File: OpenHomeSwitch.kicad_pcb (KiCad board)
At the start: 4 copper layers, 82.5 x 65.5 mm, 297 parts, among them J10 USB_C_Receptacle_USB2.0, J11 USB_C_Receptacle_USB2.0, J2 Conn_01x04, J3 Conn_01x04, J4 Micro_SD_Card_Det2, J5 Conn_01x04, J6 Extension I2C, J7 Conn_01x04, J8 Debug, J9 Extension UART, Q1 2N7002, Q10 MMBT3904, Q2 MMBT3904, Q3 MMBT3904, Q4 MMBT5401, Q5 AO3401A, Q6 MMBT5401, Q7 MMBT5401, Q8 AO3401A, Q9 MMBT5401, U1 RTL8367RB, U2 Allwinner_V3S, U3 TMI7003x, U4 TMI7003x, U5 W25Q128JVS, U6 SRV05-4, Y1 25MHz, Y2 24MHz, Y3 32.768kHz

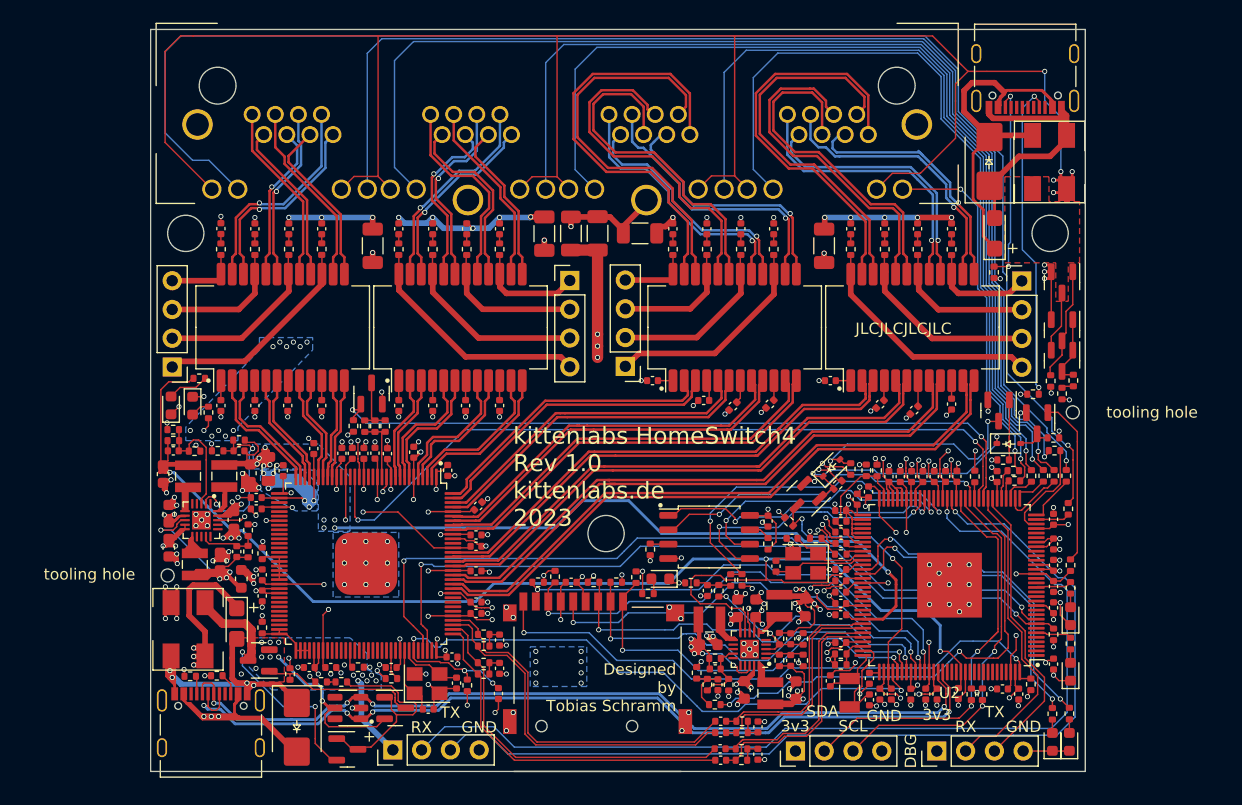
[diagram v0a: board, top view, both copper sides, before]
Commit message: Connect shield net to second USB port
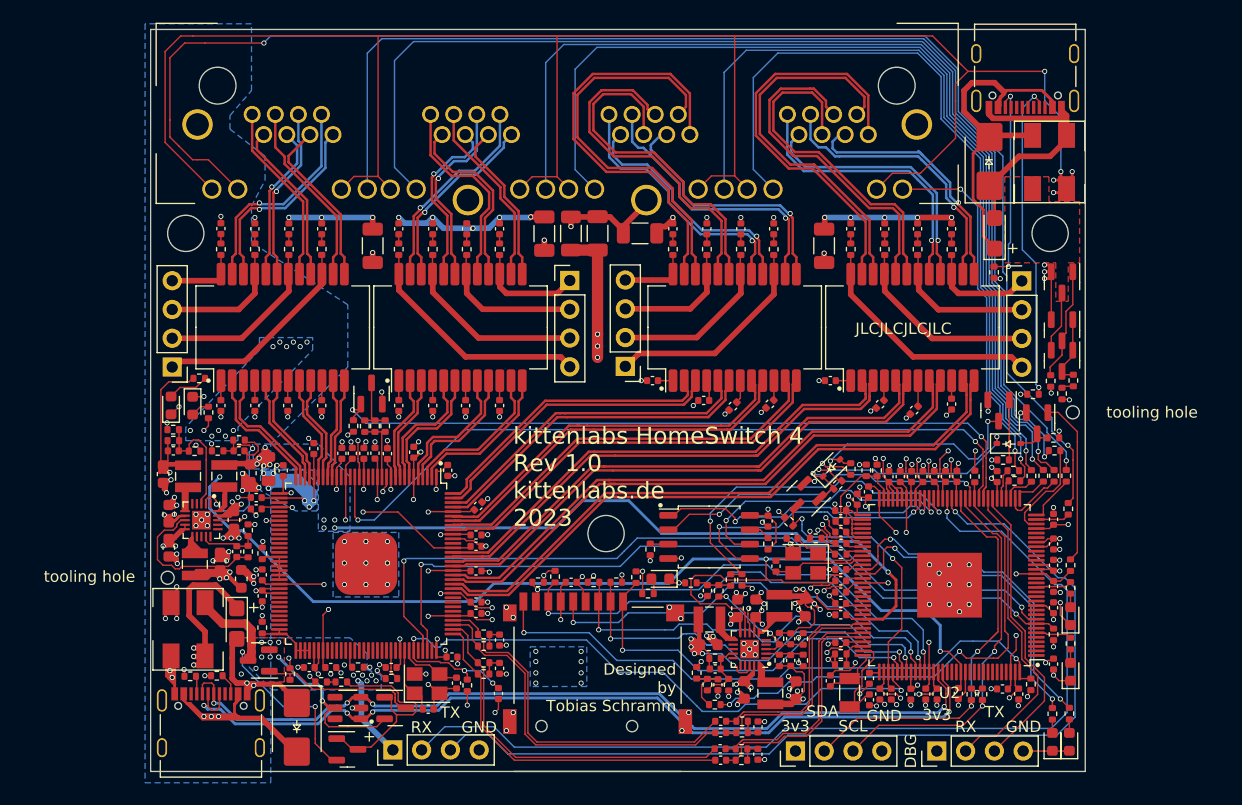
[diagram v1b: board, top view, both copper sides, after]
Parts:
- moved H5 0.20 mm to (145.0, 111.9)
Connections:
- J11 pad A7: /USB2/D- -> /USB2/D2-
- J11 pad B6: /USB2/D+ -> /USB2/D2+
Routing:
- net Net-(D5-A1): track 49.2 -> 39.7 mm
- net +3V0: track 129.7 -> 133.1 mm, vias 3 -> 4
- net GND: track 378.8 -> 375.5 mm, vias 198 -> 197
- net +3V3: track 111.4 -> 112.6 mm, vias 35 -> 34
- net Net-(J1-Pad12): track 130.2 -> 129.3 mm, vias 1 -> 2
- added copper zone on B.Cu, net Earth
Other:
- board text added: "kittenlabs HomeSwitch 4 Rev 1.0 kittenlabs.de 2023"
- board text removed: "kittenlabs HomeSwitch4 Rev 1.0 kittenlabs.de 2023"

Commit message: Fix critical DRC errors
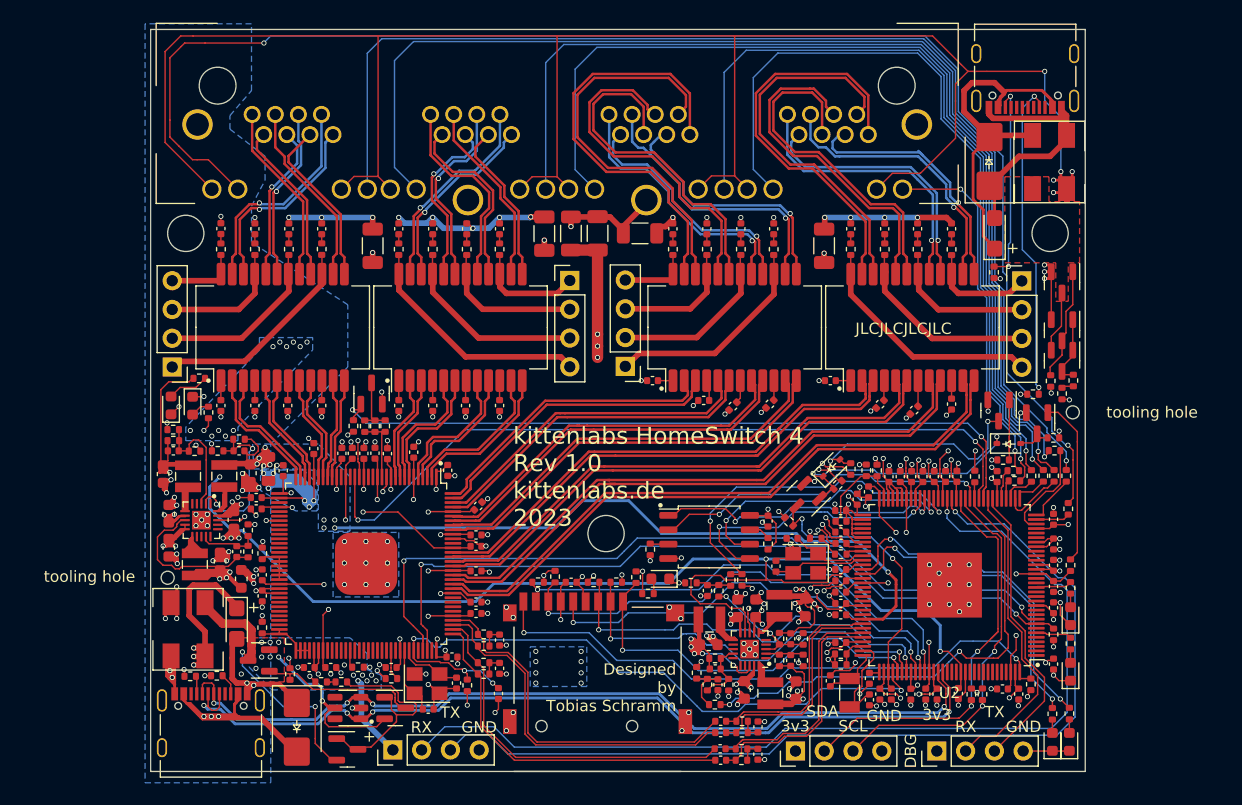
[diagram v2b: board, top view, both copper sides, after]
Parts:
- moved R21 0.08 mm to (151.3, 99.7)
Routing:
- net AVDDL: track 63.6 -> 60.5 mm, vias 14 -> 12
- net AVDDH: track 41.2 -> 39.1 mm, vias 14 -> 13
- net Net-(C32-Pad2): track 14.3 -> 14.0 mm, vias 5 -> 4
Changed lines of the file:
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@@
         (effects (font (size 1 1) (thickness 0.15)))
     )
-    (fp_text user "${REFERENCE}" (at 0 0 90) (layer "F.Fab")
-        (effects (font (size 0.25 0.25) (thickness 0.04)))
-    )
     (fp_line (start -0.107836 -0.36) (end 0.107836 -0.36)
       (stroke (width 0.12) (type solid)) (layer "F.SilkS"))
@@
   )
   (footprint "Resistor_SMD:R_0402_1005Metric" (layer "F.Cu")
-    (at 151.3 99.75 180)
+    (at 151.3 99.675 180)
     (descr "Resistor SMD 0402 (1005 Metric), square (rectangular) end terminal, IPC_7351 nominal, (Body size source: IPC-SM-782 page 72, https://www.pcb-3d.com/wordpress/wp-content/uploads/ipc-sm-782a_amendment_1_and_2.pdf), generated with kicad-footprint-generator")
     (tags "resistor")
@@
   (segment (start 211.2 80.62) (end 211.2 80.1) (width 0.127) (layer "F.Cu") (net 53))
   (segment (start 208.3 80.62) (end 208.3 80.1) (width 0.127) (layer "F.Cu") (net 53))
-  (segment (start 214.2 80.1) (end 211.2 80.1) (width 0.5) (layer "F.Cu") (net 53))
-  (segment (start 214.2 80.62) (end 214.2 80.1) (width 0.127) (layer "F.Cu") (net 53))
+  (segment (start 213.75 80.1) (end 214.25 80.6) (width 0.5) (layer "F.Cu") (net 53))
+  (segment (start 211.2 80.1) (end 213.75 80.1) (width 0.5) (layer "F.Cu") (net 53))
   (segment (start 205.3 80.62) (end 205.3 80.1) (width 0.127) (layer "F.Cu") (net 53))
   (segment (start 203 80.1) (end 203 81.1) (width 0.5) (layer "F.Cu") (net 53))
-  (via (at 214.2 80.1) (size 0.45) (drill 0.3) (layers "F.Cu" "B.Cu") (net 53))
   (via (at 205.3 80.1) (size 0.45) (drill 0.3) (layers "F.Cu" "B.Cu") (net 53))
   (via (at 203 80.1) (size 0.45) (drill 0.3) (layers "F.Cu" "B.Cu") (net 53))
@@
   (segment (start 164.4 101.9) (end 164.4 101.4) (width 0.127) (layer "F.Cu") (net 108))
   (segment (start 169.62 118.9) (end 168.8 118.9) (width 0.127) (layer "F.Cu") (net 108))
-  (segment (start 171.74 114.05) (end 172.2405 114.5505) (width 0.127) (layer "F.Cu") (net 108))
   (segment (start 152.0125 111.2125) (end 152.6 111.8) (width 0.25) (layer "F.Cu") (net 108))
   (segment (start 165.55 119.525) (end 165.55 118.3) (width 0.127) (layer "F.Cu") (net 108))
@@
   (segment (start 160.3 101.8) (end 160.3 101.5) (width 0.127) (layer "F.Cu") (net 108))
   (segment (start 169.1375 108.0625) (end 169.1 108.1) (width 0.127) (layer "F.Cu") (net 108))
-  (segment (start 173.6495 114.5505) (end 173.65 114.55) (width 0.127) (layer "F.Cu") (net 108))
   (segment (start 164.72 102.22) (end 164.4 101.9) (width 0.127) (layer "F.Cu") (net 108))
   (segment (start 170.1825 113.2625) (end 170.877796 113.2625) (width 0.127) (layer "F.Cu") (net 108))
@@
   (segment (start 151.5 111.2125) (end 151.5 111.3) (width 0.25) (layer "F.Cu") (net 108))
   (segment (start 171.6625 108.0625) (end 171.7 108.1) (width 0.127) (layer "F.Cu") (net 108))
-  (segment (start 172.2405 114.5505) (end 172.703102 114.5505) (width 0.127) (layer "F.Cu") (net 108))
   (segment (start 169.72 101.945) (end 169.705 101.945) (width 0.127) (layer "F.Cu") (net 108))
   (segment (start 151.5 111.2125) (end 151.6125 111.2125) (width 0.25) (layer "F.Cu") (net 108))
   (segment (start 170.1825 113.2625) (end 169.1375 113.2625) (width 0.127) (layer "F.Cu") (net 108))
-  (segment (start 172.703102 114.5505) (end 172.976898 114.5505) (width 0.127) (layer "F.Cu") (net 108))
   (segment (start 160.3 101.8) (end 160.1 102) (width 0.127) (layer "F.Cu") (net 108))
   (segment (start 162.32 104.08) (end 162.3 104.1) (width 0.127) (layer "F.Cu") (net 108))
   (segment (start 151.5 111.3) (end 152.6 112.4) (width 0.25) (layer "F.Cu") (net 108))
-  (segment (start 172.976898 114.5505) (end 173.6495 114.5505) (width 0.127) (layer "F.Cu") (net 108))
   (segment (start 152.6 112.4) (end 152.6 111.8) (width 0.25) (layer "F.Cu") (net 108))
   (segment (start 165.52 117.32) (end 165.5 117.3) (width 0.127) (layer "F.Cu") (net 108))
@@
   (via (at 152.6 112.4) (size 0.45) (drill 0.3) (layers "F.Cu" "B.Cu") (net 108))
   (via (at 152.6 111.8) (size 0.45) (drill 0.3) (layers "F.Cu" "B.Cu") (net 108))
-  (via (at 173.65 114.55) (size 0.45) (drill 0.3) (layers "F.Cu" "B.Cu") (net 108))
   (via (at 169.1 113.3) (size 0.45) (drill 0.3) (layers "F.Cu" "B.Cu") (net 108))
   (via (at 156 105.7) (size 0.45) (drill 0.3) (layers "F.Cu" "B.Cu") (net 108))
@@
   (segment (start 170.1825 109.2625) (end 168.5 109.2625) (width 0.127) (layer "F.Cu") (net 110))
   (segment (start 168.0375 106.0625) (end 168 106.1) (width 0.127) (layer "F.Cu") (net 110))
-  (segment (start 166.85 101.3) (end 167.35 100.8) (width 0.22) (layer "F.Cu") (net 110))
   (segment (start 170.1825 111.2625) (end 168.0375 111.2625) (width 0.127) (layer "F.Cu") (net 110))
   (segment (start 153.9 103.3625) (end 153.9 104) (width 0.25) (layer "F.Cu") (net 110))
@@
   (segment (start 156.8625 104.8625) (end 157.1 105.1) (width 0.127) (layer "F.Cu") (net 110))
   (segment (start 171.7375 115.2625) (end 171.8 115.2) (width 0.127) (layer "F.Cu") (net 110))
-  (segment (start 172.29 115.6) (end 173.65 115.6) (width 0.127) (layer "F.Cu") (net 110))
   (segment (start 166.72 104.98) (end 166.7 105) (width 0.127) (layer "F.Cu") (net 110))
   (segment (start 157.92 105.08) (end 157.9 105.1) (width 0.127) (layer "F.Cu") (net 110))
-  (segment (start 166.72 101.3) (end 166.85 101.3) (width 0.22) (layer "F.Cu") (net 110))
   (segment (start 165.3375 106.1) (end 168.5 109.2625) (width 0.127) (layer "F.Cu") (net 110))
   (segment (start 168.0375 115.2625) (end 168 115.3) (width 0.127) (layer "F.Cu") (net 110))
-  (segment (start 166.72 101.28) (end 166.75 101.25) (width 0.127) (layer "F.Cu") (net 110))
   (segment (start 154.8575 104.8625) (end 153.3625 104.8625) (width 0.127) (layer "F.Cu") (net 110))
   (segment (start 153.475 103.375) (end 153.475 102.6875) (width 0.25) (layer "F.Cu") (net 110))
   (segment (start 170.1825 115.2625) (end 171.7375 115.2625) (width 0.127) (layer "F.Cu") (net 110))
-  (segment (start 171.74 115.05) (end 172.29 115.6) (width 0.127) (layer "F.Cu") (net 110))
   (segment (start 157.92 103) (end 157.92 105.08) (width 0.127) (layer "F.Cu") (net 110))
   (segment (start 170.1825 109.2625) (end 171.7375 109.2625) (width 0.127) (layer "F.Cu") (net 110))
@@
   (via (at 168 111.3) (size 0.45) (drill 0.3) (layers "F.Cu" "B.Cu") (net 110))
   (via (at 166.7 105) (size 0.45) (drill 0.3) (layers "F.Cu" "B.Cu") (net 110))
-  (via (at 167.35 100.8) (size 0.45) (drill 0.3) (layers "F.Cu" "B.Cu") (net 110))
   (via (at 168 115.3) (size 0.45) (drill 0.3) (layers "F.Cu" "B.Cu") (net 110))
-  (via (at 173.65 115.6) (size 0.45) (drill 0.3) (layers "F.Cu" "B.Cu") (net 110))
   (via (at 153.475 102.6875) (size 0.45) (drill 0.3) (layers "F.Cu" "B.Cu") (net 110))
   (via (at 168 106.1) (size 0.45) (drill 0.3) (layers "F.Cu" "B.Cu") (net 110))
@@
   (segment (start 153.475 102.025) (end 153.923745 102.025) (width 0.25) (layer "F.Cu") (net 111))
   (segment (start 150 101.95) (end 151.85 101.95) (width 0.25) (layer "F.Cu") (net 111))
+  (segment (start 151.81 99.675) (end 152.375 99.675) (width 0.127) (layer "F.Cu") (net 111))
   (segment (start 153.4 101.3) (end 154 101.3) (width 0.5) (layer "F.Cu") (net 111))
   (segment (start 153.05 101.35) (end 152.65 101.75) (width 0.5) (layer "F.Cu") (net 111))
@@
   (segment (start 153.919445 101.8125) (end 153.6875 101.8125) (width 0.25) (layer "F.Cu") (net 111))
   (segment (start 158.72 118.325) (end 158.72 119.67) (width 0.127) (layer "F.Cu") (net 111))
-  (segment (start 152.646 99.946) (end 151.75 99.946) (width 0.127) (layer "F.Cu") (net 111))
   (segment (start 152.3 101.9) (end 152.1 101.7) (width 0.25) (layer "F.Cu") (net 111))
   (segment (start 153 100.7) (end 153 100.3) (width 0.127) (layer "F.Cu") (net 111))
   (segment (start 205.4075 115.5575) (end 204.97 115.12) (width 0.127) (layer "F.Cu") (net 111))
+  (segment (start 152.375 99.675) (end 152.646 99.946) (width 0.127) (layer "F.Cu") (net 111))
   (segment (start 158.7625 112.4625) (end 158.8 112.5) (width 0.127) (layer "F.Cu") (net 111))
   (segment (start 209.3 114.4) (end 209.3 112.5) (width 0.25) (layer "F.Cu") (net 111))
@@
   )
   (zone (net 121) (net_name "VBUS") (layer "B.Cu") (hatch edge 0.5)
-    (priority 1)
+    (priority 10)
     (connect_pads thru_hole_only (clearance 0.127))
     (min_thickness 0.127) (filled_areas_thickness no)
